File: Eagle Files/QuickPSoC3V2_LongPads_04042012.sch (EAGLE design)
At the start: 25 parts, among them SW1 PSHBTTN, X1 USB-MINIB-5PIN

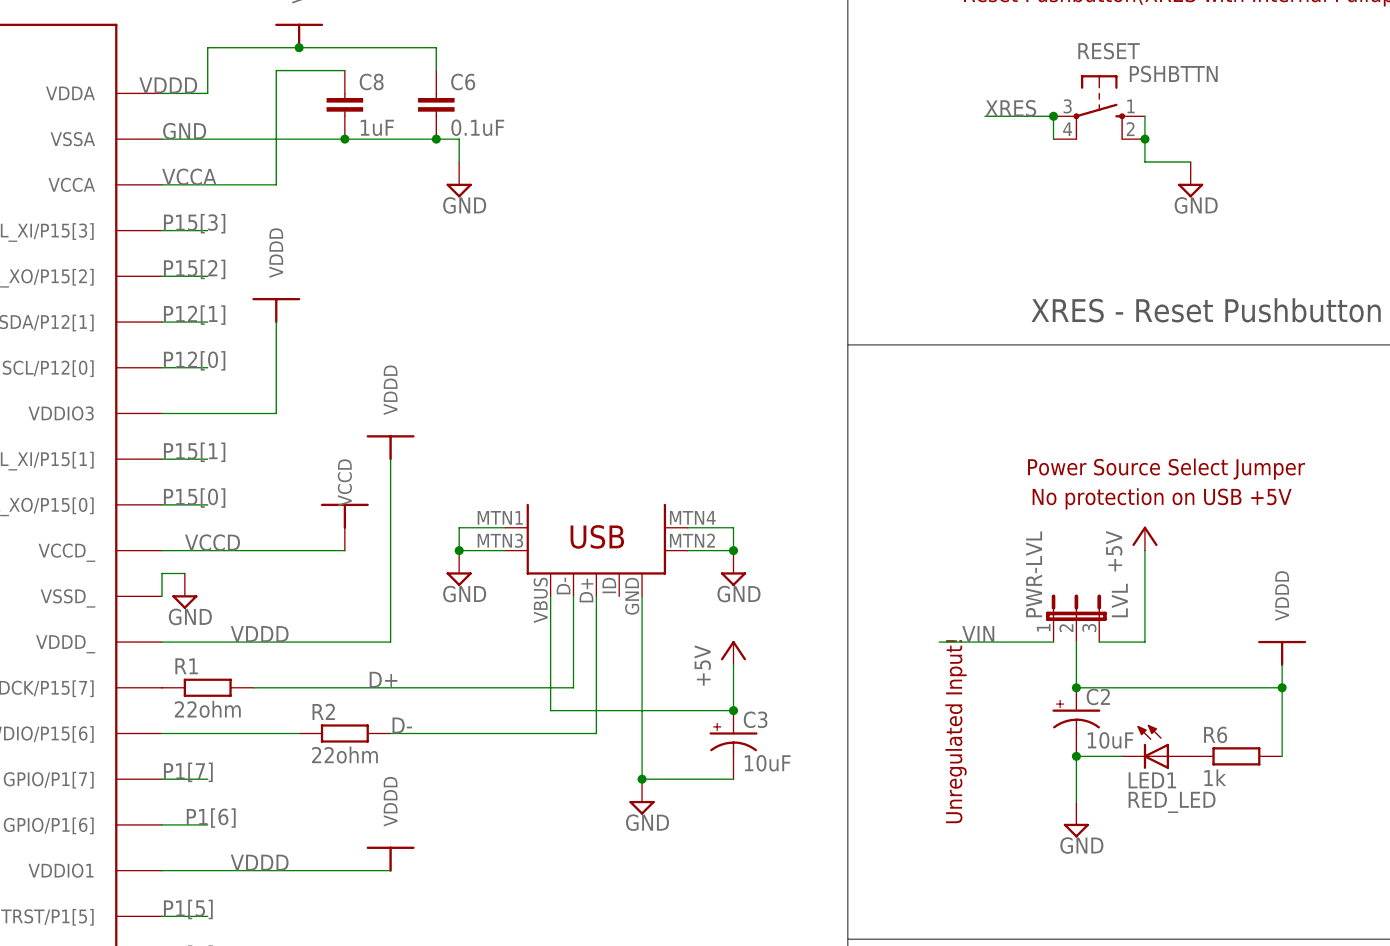
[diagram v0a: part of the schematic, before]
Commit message: Removed the 22ohm resistors on the USB lines,since it works just fine without them. Removed 10uF cap on USB +5V line. Added MiniProg3 insertion indication on silkscreen.
Edited gitignore to ignore *.s#* and *.b#* files.
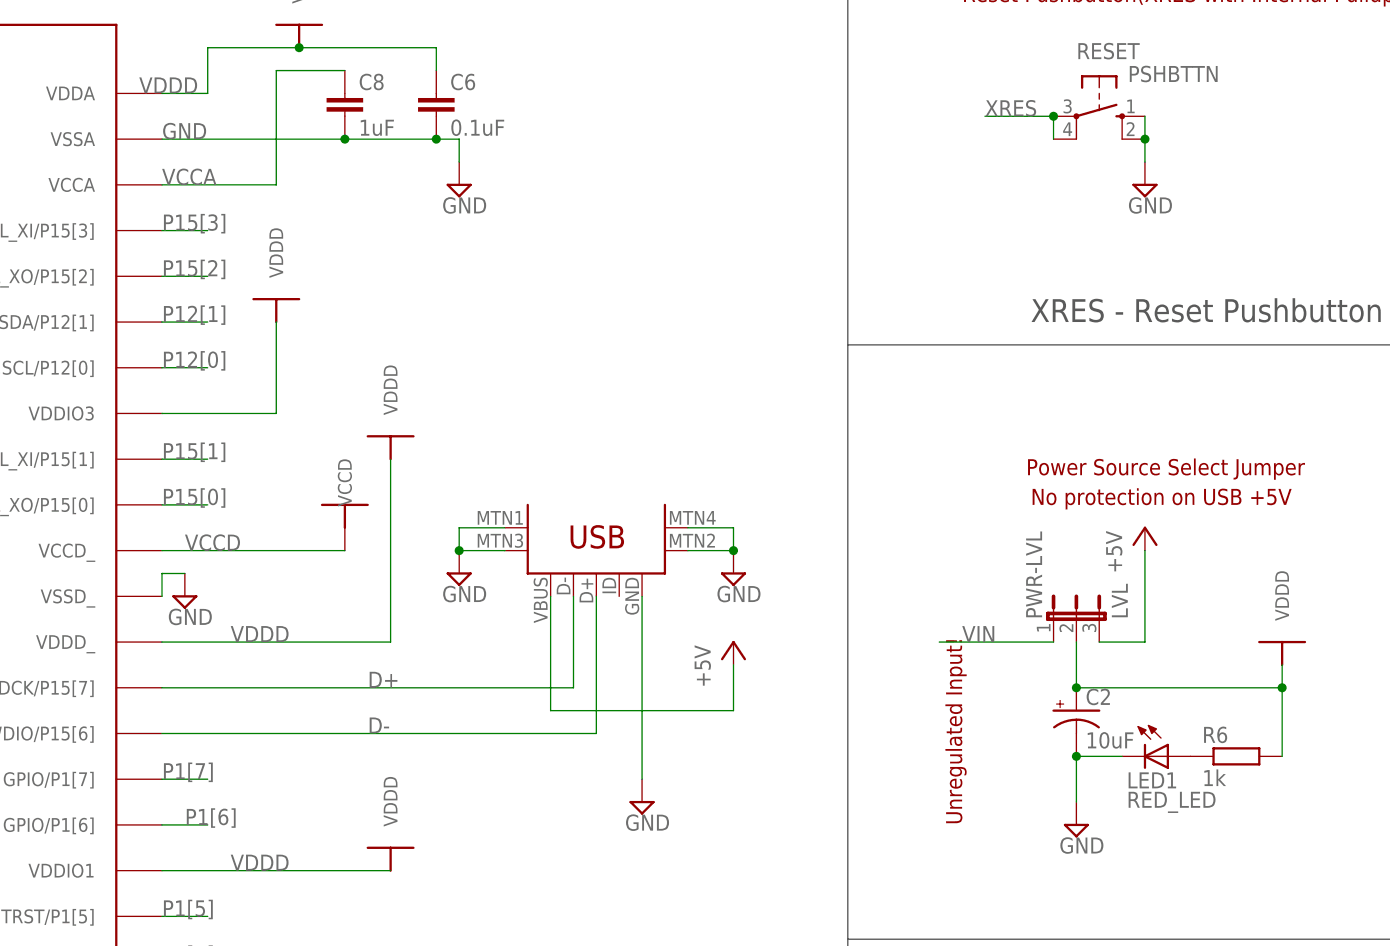
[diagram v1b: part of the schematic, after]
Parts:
- removed C3: 10uF, SparkFun:CAP_POLPTH2
- removed R1, R2: 22ohm, rcl:R-EU_M0805
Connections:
- removed net N$3: R2.1, U$1.D+,SWDIO/P15[6]
- removed net N$4: R1.1, U$1.D-,SWDCK/P15[7]
- net +5V: no longer C3.+
- net D+: now also U$1.D-,SWDCK/P15[7]; no longer R1.2
- net D-: now also U$1.D+,SWDIO/P15[6]; no longer R2.2
- net GND: no longer C3.-
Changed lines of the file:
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@@
 <?xml version="1.0" encoding="utf-8"?>
 <!DOCTYPE eagle SYSTEM "eagle.dtd">
-<eagle version="6.1">
+<eagle version="6.2">
 <drawing>
 <settings>
@@
 <part name="C5" library="rcl" deviceset="C-EU" device="C0805K" value="1uF"/>
 <part name="X1" library="SparkFun" deviceset="USB-MINIB" device="-5PIN"/>
-<part name="R1" library="rcl" deviceset="R-EU_" device="M0805" value="22ohm"/>
-<part name="R2" library="rcl" deviceset="R-EU_" device="M0805" value="22ohm"/>
 <part name="RESET" library="switch-omron" deviceset="10-XX" device="" value="PSHBTTN"/>
 <part name="SUPPLY1" library="supply2" deviceset="GND" device=""/>
@@
 <part name="H3" library="holes" deviceset="MOUNT-PAD-ROUND" device="2.8"/>
 <part name="FRAME1" library="SparkFun" deviceset="FRAME-A3" device=""/>
-<part name="C3" library="SparkFun" deviceset="CAP_POL" device="PTH2" value="10uF"/>
 <part name="SUPPLY10" library="supply2" deviceset="GND" device=""/>
 <part name="R3" library="rcl" deviceset="R-EU_" device="M0805" value="1k"/>
@@
 <instance part="C5" gate="G$1" x="-33.02" y="83.82"/>
 <instance part="X1" gate="G$1" x="106.68" y="66.04" rot="R90"/>
-<instance part="R1" gate="G$1" x="58.42" y="53.34"/>
-<instance part="R2" gate="G$1" x="73.66" y="48.26"/>
 <instance part="RESET" gate="1" x="157.48" y="116.84" rot="R270"/>
 <instance part="SUPPLY1" gate="GND" x="106.68" y="40.64"/>
@@
 <instance part="SUPPLY7" gate="GND" x="-33.02" y="73.66"/>
 <instance part="SUPPLY8" gate="GND" x="-20.32" y="78.74"/>
-<instance part="SUPPLY9" gate="GND" x="167.64" y="109.22"/>
+<instance part="SUPPLY9" gate="GND" x="162.56" y="109.22"/>
 <instance part="C2" gate="G$1" x="154.94" y="50.8"/>
 <instance part="P+1" gate="1" x="162.56" y="71.12"/>
@@
 <instance part="H3" gate="G$1" x="236.22" y="114.3" rot="R180"/>
 <instance part="FRAME1" gate="G$1" x="-48.26" y="-119.38"/>
-<instance part="C3" gate="G$1" x="116.84" y="48.26"/>
 <instance part="SUPPLY10" gate="GND" x="243.84" y="121.92" rot="R90"/>
 <instance part="R3" gate="G$1" x="66.04" y="-33.02" rot="R180"/>
@@
 </segment>
 </net>
-<net name="N$3" class="0">
-<segment>
-<wire x1="68.58" y1="48.26" x2="53.34" y2="48.26" width="0.1524" layer="91"/>
-<pinref part="U$1" gate="G$1" pin="D+,SWDIO/P15[6]"/>
-<pinref part="R2" gate="G$1" pin="1"/>
-</segment>
-</net>
-<net name="N$4" class="0">
-<segment>
-<pinref part="U$1" gate="G$1" pin="D-,SWDCK/P15[7]"/>
-<pinref part="R1" gate="G$1" pin="1"/>
-</segment>
-</net>
 <net name="XRES" class="0">
 <segment>
@@
 <net name="D-" class="0">
 <segment>
-<wire x1="78.74" y1="48.26" x2="101.6" y2="48.26" width="0.1524" layer="91"/>
 <wire x1="101.6" y1="48.26" x2="101.6" y2="63.5" width="0.1524" layer="91"/>
-<label x="78.74" y="48.26" size="1.778" layer="95"/>
-<pinref part="R2" gate="G$1" pin="2"/>
+<label x="76.2" y="48.26" size="1.778" layer="95"/>
 <pinref part="X1" gate="G$1" pin="D+"/>
+<wire x1="101.6" y1="48.26" x2="53.34" y2="48.26" width="0.1524" layer="91"/>
+<pinref part="U$1" gate="G$1" pin="D+,SWDIO/P15[6]"/>
 </segment>
 </net>
 <net name="D+" class="0">
 <segment>
-<wire x1="63.5" y1="53.34" x2="99.06" y2="53.34" width="0.1524" layer="91"/>
+<wire x1="53.34" y1="53.34" x2="99.06" y2="53.34" width="0.1524" layer="91"/>
 <wire x1="99.06" y1="53.34" x2="99.06" y2="63.5" width="0.1524" layer="91"/>
 <label x="76.2" y="53.34" size="1.778" layer="95"/>
-<pinref part="R1" gate="G$1" pin="2"/>
 <pinref part="X1" gate="G$1" pin="D-"/>
+<pinref part="U$1" gate="G$1" pin="D-,SWDCK/P15[7]"/>
 </segment>
 </net>
@@
 <segment>
 <wire x1="106.68" y1="43.18" x2="106.68" y2="63.5" width="0.1524" layer="91"/>
-<wire x1="106.68" y1="43.18" x2="116.84" y2="43.18" width="0.1524" layer="91"/>
-<junction x="106.68" y="43.18"/>
 <pinref part="X1" gate="G$1" pin="GND"/>
 <pinref part="SUPPLY1" gate="GND" pin="GND"/>
-<pinref part="C3" gate="G$1" pin="-"/>
 </segment>
 <segment>
@@
 <wire x1="162.56" y1="116.84" x2="162.56" y2="114.3" width="0.1524" layer="91"/>
 <wire x1="162.56" y1="114.3" x2="162.56" y2="111.76" width="0.1524" layer="91"/>
-<wire x1="162.56" y1="111.76" x2="167.64" y2="111.76" width="0.1524" layer="91"/>
 <junction x="162.56" y="114.3"/>
 <pinref part="RESET" gate="1" pin="S"/>
@@
 <wire x1="96.52" y1="50.8" x2="116.84" y2="50.8" width="0.1524" layer="91"/>
 <wire x1="116.84" y1="55.88" x2="116.84" y2="50.8" width="0.1524" layer="91"/>
-<junction x="116.84" y="50.8"/>
 <pinref part="P+3" gate="1" pin="+5V"/>
 <pinref part="X1" gate="G$1" pin="VBUS"/>
-<pinref part="C3" gate="G$1" pin="+"/>
-</segment>
-</net>
+</segment>
+</net>
